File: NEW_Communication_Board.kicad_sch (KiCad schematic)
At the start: 67 parts, among them J1 USB_IN, J2 IMU, J4 XM_conn, J5 HUB-3, J6 HUB-4, U1 FE1.1s, U2 FT232RL, U3 FT232RL, U4 L7805, U5 FT232RL, U6 FT232RL, U8 ST485E, Y1 Crystal 12MHz - ECS

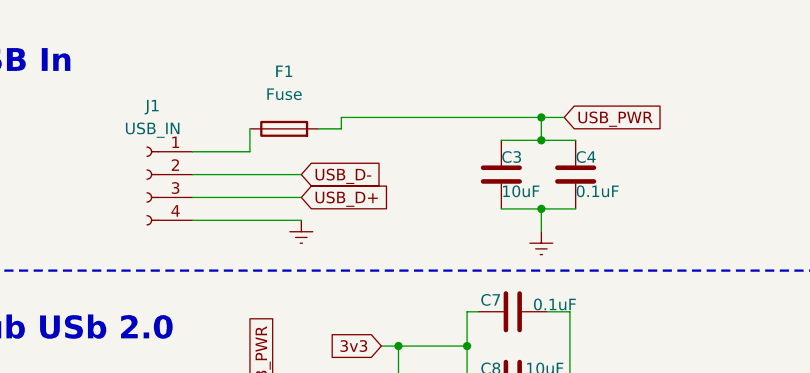
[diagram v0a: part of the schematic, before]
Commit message: Changing the LDO, and correcting the Edge.Cuts
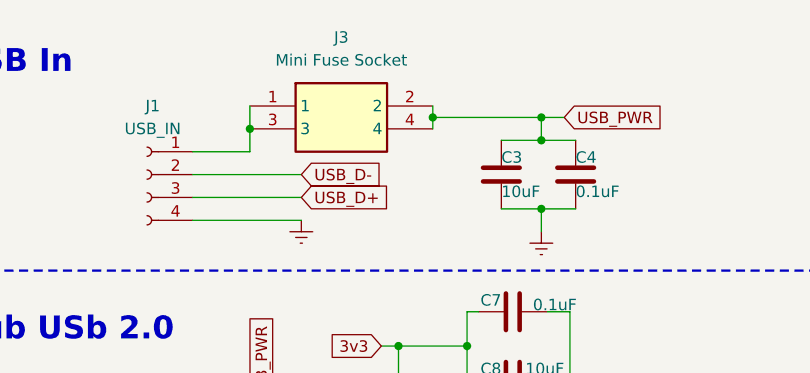
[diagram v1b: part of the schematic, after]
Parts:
- removed F1: Fuse, Fuse:Fuseholder_Cylinder-5x20mm_Schurter_0031_8201_Horizontal_Open, symbol Device:Fuse
- added J3: Mini Fuse Socket, Humanoid:Mini Fuse Socket, symbol Humanoid:Mini_Fuse_Socket
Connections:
- net USB_PWR: now also J3.2, J3.4
- net at J1.1 (Pin_1): now also J3.1, J3.3
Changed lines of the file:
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@@
 	)
 	(junction
+		(at 66.04 22.86)
+		(diameter 0)
+		(color 0 0 0 0)
+	)
+	(junction
 		(at 149.86 21.59)
 		(diameter 0)
@@
 	)
 	(junction
+		(at 45.72 24.13)
+		(diameter 0)
+		(color 0 0 0 0)
+	)
+	(junction
 		(at 149.86 27.94)
 		(diameter 0)
@@
 	)
 	(junction
-		(at 78.105 22.86)
-		(diameter 0)
-		(color 0 0 0 0)
-	)
-	(junction
 		(at 45.72 191.77)
 		(diameter 0)
@@
 	)
 	(junction
+		(at 78.105 22.86)
+		(diameter 0)
+		(color 0 0 0 0)
+	)
+	(junction
 		(at 223.52 161.29)
 		(diameter 0)
@@
 	(wire
 		(pts
-			(xy 55.88 22.86) (xy 78.105 22.86)
-		)
-		(stroke
-			(width 0)
-			(type default)
-		)
-	)
-	(wire
-		(pts
 			(xy 134.62 44.45) (xy 138.43 44.45)
 		)
@@
 	(wire
 		(pts
-			(xy 69.85 62.865) (xy 69.85 66.675)
+			(xy 78.105 22.86) (xy 80.645 22.86)
 		)
 		(stroke
@@
 	(wire
 		(pts
-			(xy 186.69 44.45) (xy 186.69 57.15)
+			(xy 69.85 62.865) (xy 69.85 66.675)
 		)
 		(stroke
@@
 	(wire
 		(pts
-			(xy 182.88 77.47) (xy 222.25 77.47)
+			(xy 186.69 44.45) (xy 186.69 57.15)
 		)
 		(stroke
@@
 	(wire
 		(pts
-			(xy 53.34 24.13) (xy 55.88 24.13)
+			(xy 182.88 77.47) (xy 222.25 77.47)
 		)
 		(stroke
@@
 	(wire
 		(pts
+			(xy 66.04 22.86) (xy 66.04 24.13)
+		)
+		(stroke
+			(width 0)
+			(type default)
+		)
+	)
+	(wire
+		(pts
 			(xy 116.84 133.35) (xy 115.57 133.35)
 		)
@@
 	(wire
 		(pts
+			(xy 66.04 21.59) (xy 66.04 22.86)
+		)
+		(stroke
+			(width 0)
+			(type default)
+		)
+	)
+	(wire
+		(pts
 			(xy 69.85 44.45) (xy 71.12 44.45)
 		)
@@
 	(wire
 		(pts
-			(xy 80.645 22.86) (xy 78.105 22.86)
-		)
-		(stroke
-			(width 0)
-			(type default)
-		)
-	)
-	(wire
-		(pts
 			(xy 86.36 179.07) (xy 92.71 179.07)
 		)
@@
 	(wire
 		(pts
-			(xy 55.88 24.13) (xy 55.88 22.86)
-		)
-		(stroke
-			(width 0)
-			(type default)
-		)
-	)
-	(wire
-		(pts
 			(xy 69.85 59.055) (xy 69.85 62.865)
 		)
@@
 	(wire
 		(pts
+			(xy 45.72 24.13) (xy 45.72 21.59)
+		)
+		(stroke
+			(width 0)
+			(type default)
+		)
+	)
+	(wire
+		(pts
 			(xy 55.88 68.58) (xy 55.88 69.85)
 		)
@@
 	(wire
 		(pts
+			(xy 66.04 22.86) (xy 78.105 22.86)
+		)
+		(stroke
+			(width 0)
+			(type default)
+		)
+	)
+	(wire
+		(pts
 			(xy 85.725 115.57) (xy 85.725 123.825)
 		)
@@
 	)
 	(symbol
-		(lib_id "Device:Fuse")
-		(at 49.53 24.13 90)
-		(unit 1)
-		(exclude_from_sim no)
-		(in_bom yes)
-		(on_board yes)
-		(dnp no)
-		(fields_autoplaced yes)
-		(property "Reference" "F1"
-			(at 49.53 17.78 90)
-			(effects
-				(font
-					(size 1.27 1.27)
-				)
-			)
-		)
-		(property "Value" "Fuse"
-			(at 49.53 20.32 90)
-			(effects
-				(font
-					(size 1.27 1.27)
-				)
-			)
-		)
-		(property "Footprint" "Fuse:Fuseholder_Cylinder-5x20mm_Schurter_0031_8201_Horizontal_Open"
-			(at 49.53 25.908 90)
-			(effects
-				(font
-					(size 1.27 1.27)
-				)
-				(hide yes)
-			)
-		)
-		(property "Datasheet" "~"
-			(at 49.53 24.13 0)
-			(effects
-				(font
-					(size 1.27 1.27)
-				)
-				(hide yes)
-			)
-		)
-		(property "Description" "Fuse"
-			(at 49.53 24.13 0)
-			(effects
-				(font
-					(size 1.27 1.27)
-				)
-				(hide yes)
-			)
-		)
-		(pin "2"
-		)
-		(pin "1"
-		)
-		(instances
-			(project "NEW_Communication_Board"
-				(path "/541a1e5d-fb77-41a5-941f-f895851ed477"
-					(reference "F1")
-					(unit 1)
-				)
-			)
-		)
-	)
-	(symbol
 		(lib_id "Interface_USB:FT232RL")
 		(at 148.59 151.13 0)
@@
 					(unit 1)
 				)
+			)
+		)
+	)
+	(symbol
+		(lib_id "Humanoid:Mini_Fuse_Socket")
+		(at 45.72 21.59 0)
+		(unit 1)
+		(exclude_from_sim no)
+		(in_bom yes)
+		(on_board yes)
+		(dnp no)
+		(fields_autoplaced yes)
+		(property "Reference" "J3"
+			(at 55.88 13.97 0)
+			(effects
+				(font
+					(size 1.27 1.27)
+				)
+			)
+		)
+		(property "Value" "Mini Fuse Socket"
+			(at 55.88 16.51 0)
+			(effects
+				(font
+					(size 1.27 1.27)
+				)
+			)
+		)
+		(property "Footprint" "Humanoid:Mini Fuse Socket"
+			(at 62.23 116.51 0)
+			(effects
+				(font
+					(size 1.27 1.27)
+				)
+				(justify left top)
+				(hide yes)
+			)
+		)
+		(property "Datasheet" "http://www.keyelco.com/product-pdf.cfm?p=296"
+			(at 62.23 216.51 0)
+			(effects
+				(font
+					(size 1.27 1.27)
+				)
+				(justify left top)
+				(hide yes)
+			)
+		)
+		(property "Description" "THM 2 in 1 Auto Blade Holder P/N 3557-2"
+			(at 45.72 21.59 0)
+			(effects
+				(font
+					(size 1.27 1.27)
+				)
+				(hide yes)
+			)
+		)
+		(property "Height" ""
+			(at 62.23 416.51 0)
+			(effects
+				(font
+					(size 1.27 1.27)
+				)
+				(justify left top)
+				(hide yes)
+			)
+		)
+		(property "Mouser Part Number" "534-3557-2"
+			(at 62.23 516.51 0)
+			(effects
+				(font
+					(size 1.27 1.27)
+				)
+				(justify left top)
+				(hide yes)
+			)
+		)
+		(property "Mouser Price/Stock" "https://www.mouser.co.uk/ProductDetail/Keystone-Electronics/3557-2?qs=cxy41lVAGV%2FfbyASjpXK1g%3D%3D"
+			(at 62.23 616.51 0)
+			(effects
+				(font
+					(size 1.27 1.27)
+				)
+				(justify left top)
+				(hide yes)
+			)
+		)
+		(property "Manufacturer_Name" "Keystone Electronics"
+			(at 62.23 716.51 0)
+			(effects
+				(font
+					(size 1.27 1.27)
+				)
+				(justify left top)
+				(hide yes)
+			)
+		)
+		(property "Manufacturer_Part_Number" "3557-2"
+			(at 62.23 816.51 0)
+			(effects
+				(font
+					(size 1.27 1.27)
+				)
+				(justify left top)
+				(hide yes)
+			)
+		)
+		(pin "3"
+		)
+		(pin "1"
+		)
+		(pin "2"
+		)
+		(pin "4"
+		)
+		(instances
+			(project "NEW_Communication_Board"
+				(path "/541a1e5d-fb77-41a5-941f-f895851ed477"
+					(reference "J3")
+					(unit 1)
+				)
